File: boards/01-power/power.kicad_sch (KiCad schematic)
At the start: 3 parts, among them J1 CONN_DF40_100P_F, J2 CONN_USB_C_M, P1 MAG_RB1_125BAG1A

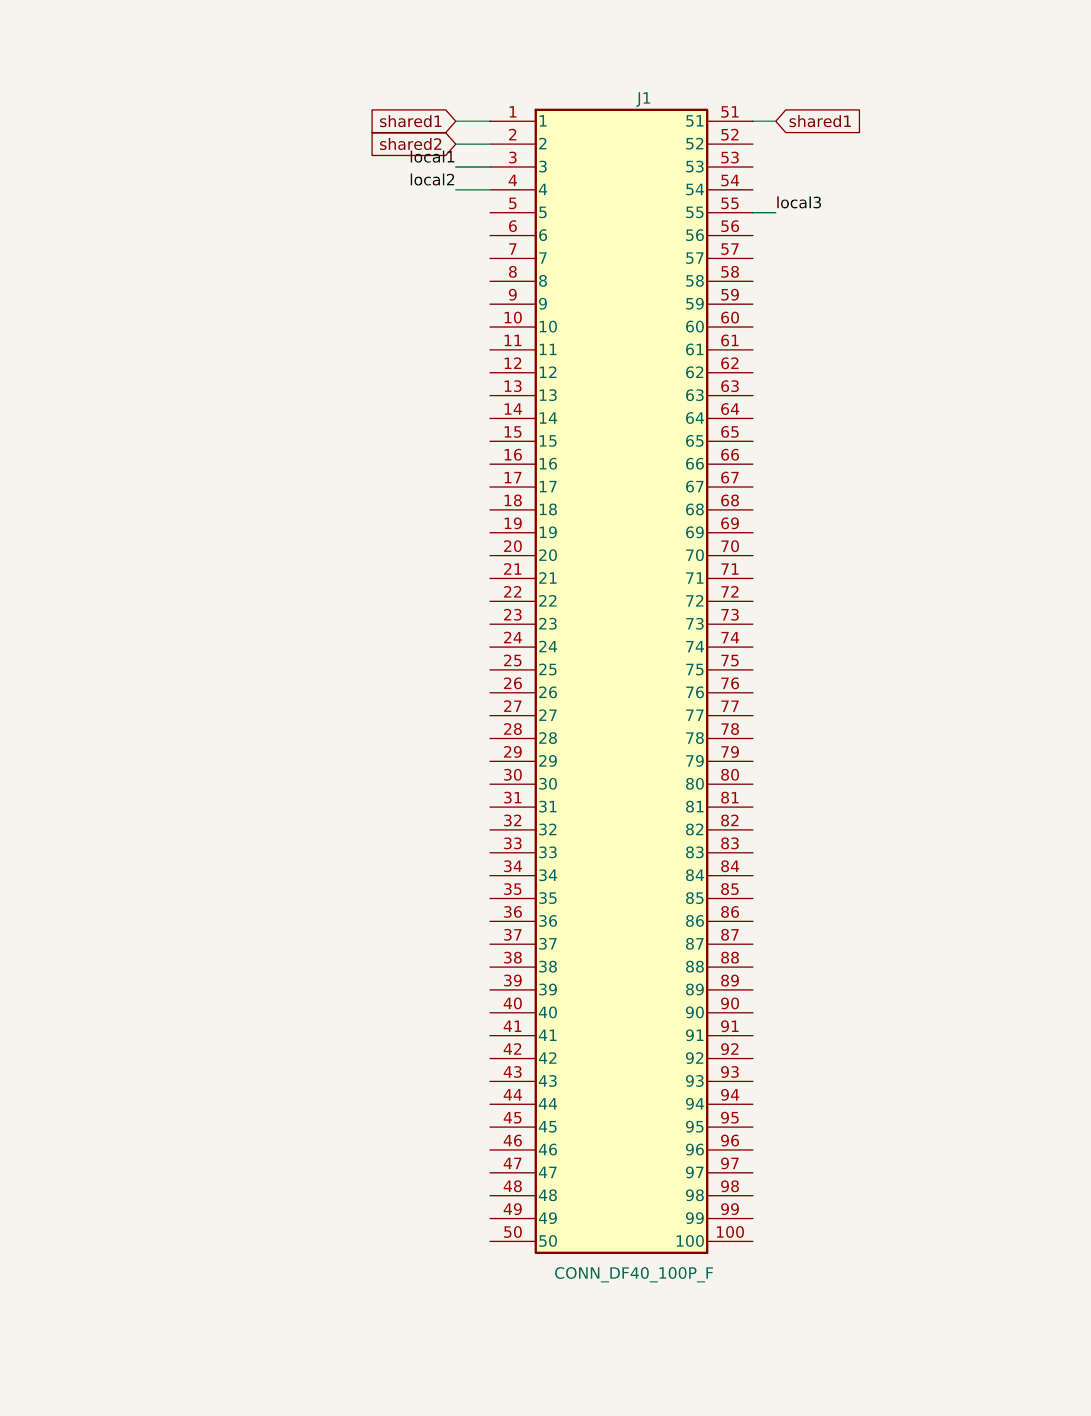
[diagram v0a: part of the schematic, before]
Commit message: Update connector pinout
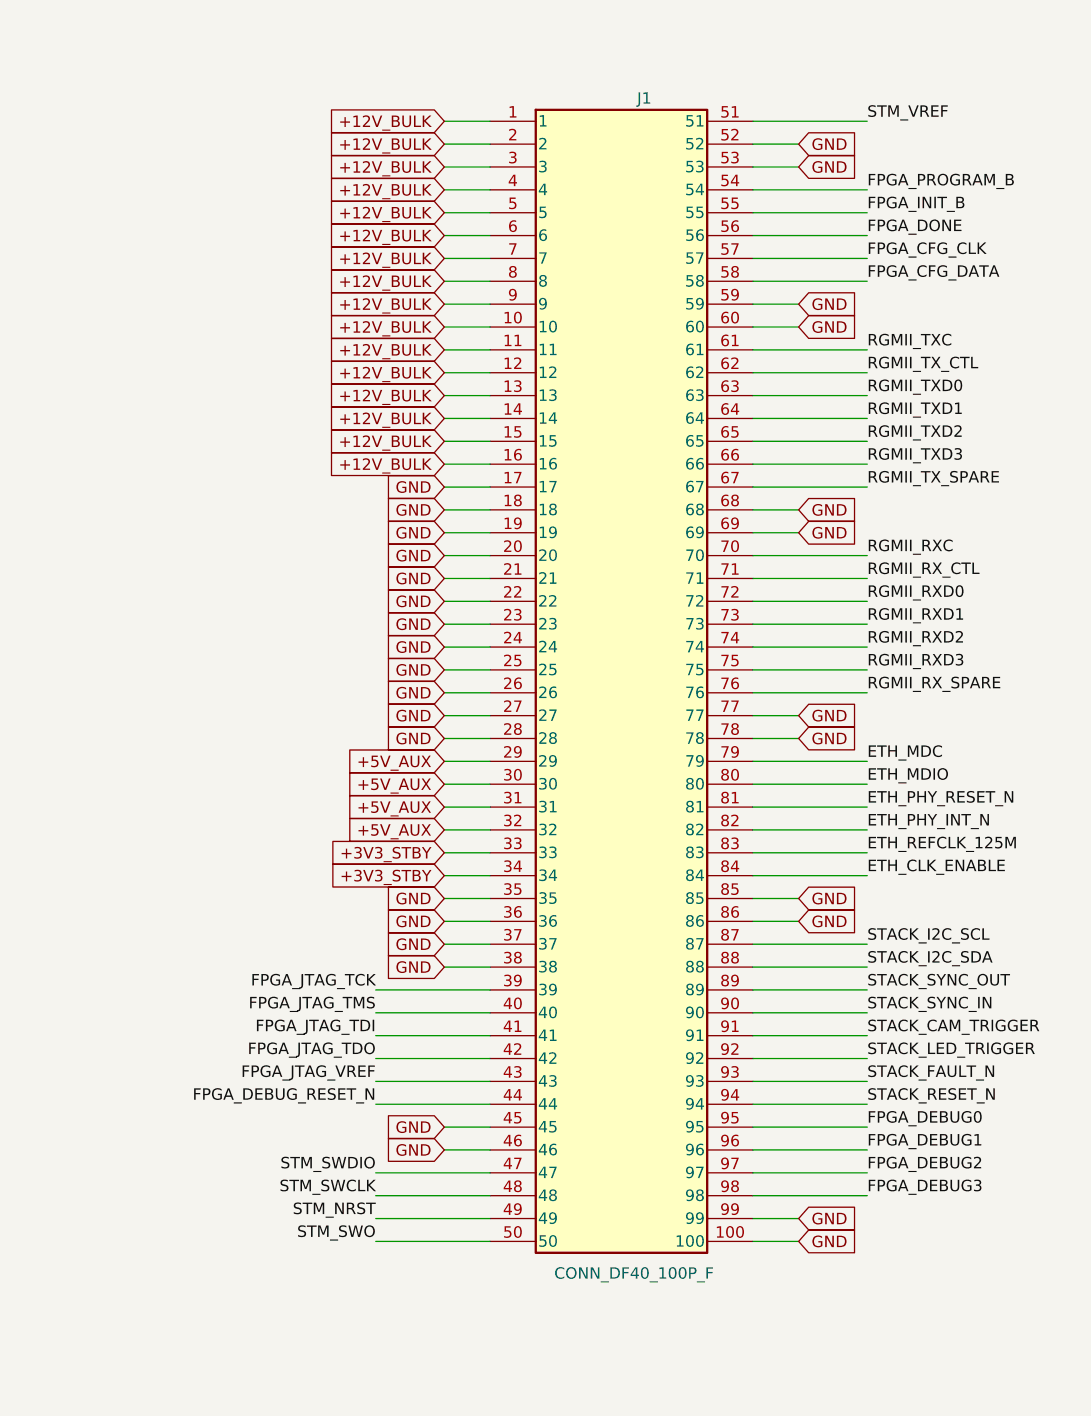
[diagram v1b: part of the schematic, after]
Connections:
- net local1 is gone; now on net +12V_BULK: J1.3
- net local2 is gone; now on net +12V_BULK: J1.4
- net shared2 is gone; now on net +12V_BULK: J1.2
- net +12V_BULK: now reaches J1.10
- net +12V_BULK: now also J1.1, J1.11, J1.12, J1.13, J1.14, J1.15, J1.16, J1.5, J1.6, J1.7, J1.8, J1.9
- net GND: now reaches J1.100
- net GND: now also J1.17, J1.18, J1.19, J1.20, J1.21, J1.22, J1.23, J1.24, J1.25, J1.26, J1.27, J1.28, J1.35, J1.36, J1.37, J1.38, J1.45, J1.46, J1.52, J1.53, J1.59, J1.60, J1.68, J1.69, J1.77, J1.78, J1.85, J1.86, J1.99
- net +5V_AUX: now reaches J1.29
- net +5V_AUX: now also J1.30, J1.31, J1.32
- net +3V3_STBY: now reaches J1.33
- net +3V3_STBY: now also J1.34
- net FPGA_JTAG_TCK: now reaches J1.39
- net FPGA_JTAG_TMS: now reaches J1.40
- net FPGA_JTAG_TDI: now reaches J1.41
- net FPGA_JTAG_TDO: now reaches J1.42
- net FPGA_JTAG_VREF: now reaches J1.43
- net FPGA_DEBUG_RESET_N: now reaches J1.44
- net STM_SWDIO: now reaches J1.47
- net STM_SWCLK: now reaches J1.48
- net STM_NRST: now reaches J1.49
- net STM_SWO: now reaches J1.50
- net FPGA_PROGRAM_B: now reaches J1.54
- net FPGA_DONE: now reaches J1.56
- net FPGA_CFG_CLK: now reaches J1.57
- net FPGA_CFG_DATA: now reaches J1.58
- net RGMII_TXC: now reaches J1.61
- net RGMII_TX_CTL: now reaches J1.62
- net RGMII_TXD0: now reaches J1.63
- net RGMII_TXD1: now reaches J1.64
- net RGMII_TXD2: now reaches J1.65
- net RGMII_TXD3: now reaches J1.66
- net RGMII_TX_SPARE: now reaches J1.67
- net RGMII_RXC: now reaches J1.70
- net RGMII_RX_CTL: now reaches J1.71
- net RGMII_RXD0: now reaches J1.72
- net RGMII_RXD1: now reaches J1.73
- net RGMII_RXD2: now reaches J1.74
- net RGMII_RXD3: now reaches J1.75
- net RGMII_RX_SPARE: now reaches J1.76
- net ETH_MDC: now reaches J1.79
- net ETH_MDIO: now reaches J1.80
- net ETH_PHY_RESET_N: now reaches J1.81
- net ETH_PHY_INT_N: now reaches J1.82
- net ETH_REFCLK_125M: now reaches J1.83
- net ETH_CLK_ENABLE: now reaches J1.84
- net STACK_I2C_SCL: now reaches J1.87
- net STACK_I2C_SDA: now reaches J1.88
- net STACK_SYNC_OUT: now reaches J1.89
- net STACK_SYNC_IN: now reaches J1.90
- net STACK_CAM_TRIGGER: now reaches J1.91
- net STACK_LED_TRIGGER: now reaches J1.92
- net STACK_FAULT_N: now reaches J1.93
- net STACK_RESET_N: now reaches J1.94
- net FPGA_DEBUG0: now reaches J1.95
- net FPGA_DEBUG1: now reaches J1.96
- net FPGA_DEBUG2: now reaches J1.97
- net FPGA_DEBUG3: now reaches J1.98
- net local3 renamed FPGA_INIT_B
- net shared1 renamed STM_VREF
- net STM_VREF: no longer J1.1
